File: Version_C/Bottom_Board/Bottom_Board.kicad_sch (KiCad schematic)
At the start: 9 parts, among them J1 Conn_02x03_Top_Bottom, J2 Conn_02x03_Top_Bottom, J3 Screw_Terminal_01x06, J5 DIN-5, SW2 SW_DIP_x04

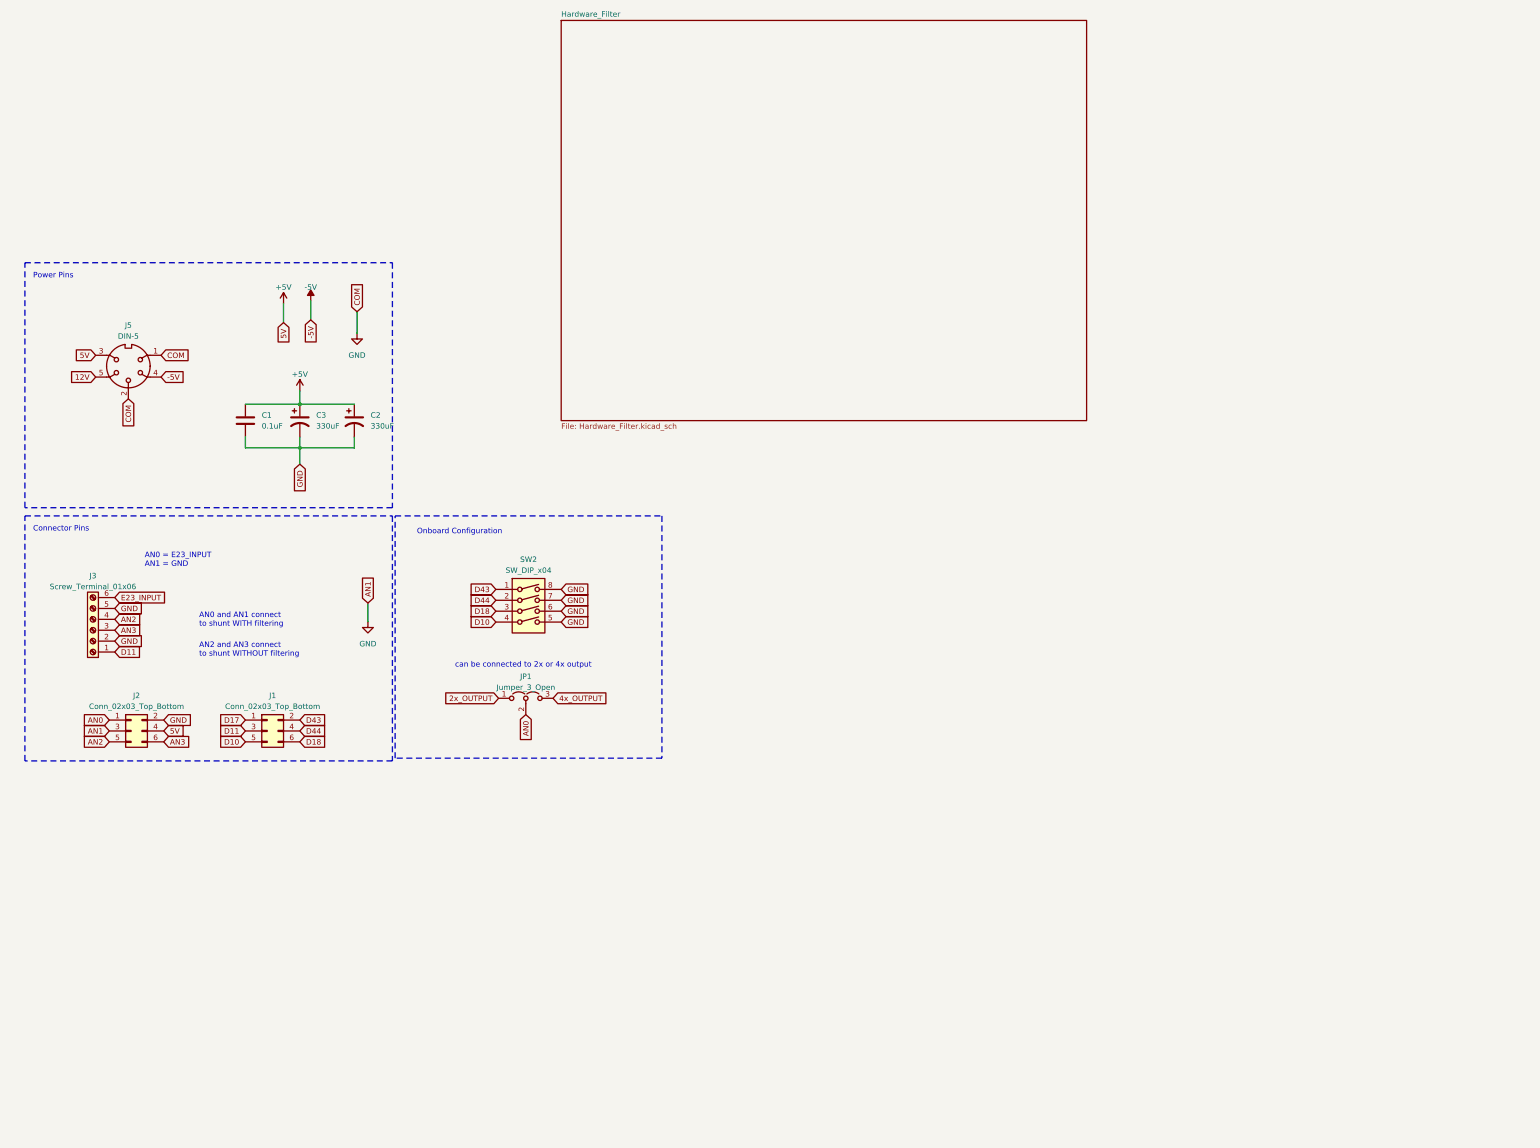
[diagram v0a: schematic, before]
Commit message: fixed directory overwrite
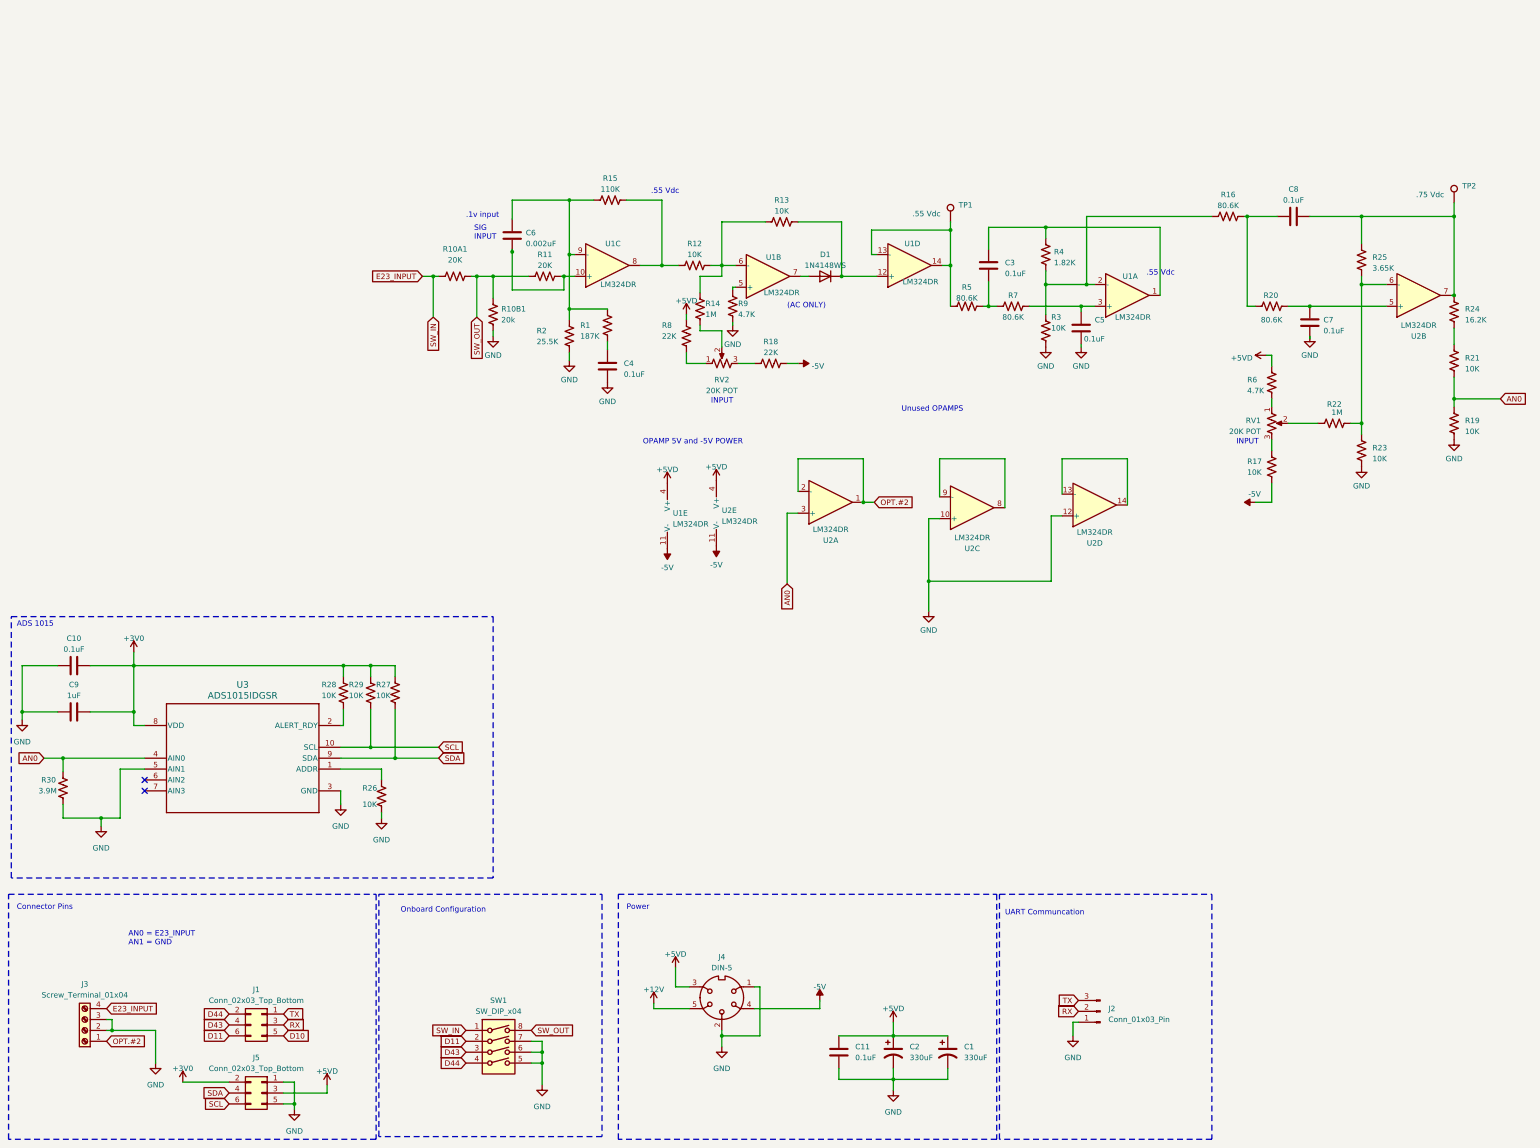
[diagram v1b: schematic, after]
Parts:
- removed J3: Screw_Terminal_01x06, Connector_Phoenix_MSTB:PhoenixContact_MSTBA_2,5_6-G-5,08_1x06_P5.08mm_Horizontal, symbol Connector:Screw_Terminal_01x06
- removed JP1: Jumper_3_Open, Connector_PinHeader_2.54mm:PinHeader_1x03_P2.54mm_Vertical, symbol Jumper:Jumper_3_Open
- added C10, C3, C4, C5, C7, C8: 0.1uF, Capacitor_SMD:C_0603_1608Metric, symbol Device:C
- added C6: 0.002uF, Capacitor_SMD:C_0603_1608Metric, symbol Device:C
- added C9: 1uF, Capacitor_SMD:C_0603_1608Metric, symbol Device:C
- added D1: 1N4148WS, bot_lib:Diode_1N4148WS, symbol Diode:1N914
- added J2: Conn_01x03_Pin, Connector_PinHeader_2.54mm:PinHeader_1x03_P2.54mm_Vertical, symbol Connector:Conn_01x03_Pin
- added J3: Screw_Terminal_01x04, bot_lib:Terminal_Strip_4_Pin, symbol Connector:Screw_Terminal_01x04
- added R1: 187K, Resistor_SMD:R_0603_1608Metric, symbol Device:R_US
- added R10A1, R11: 20K, Resistor_SMD:R_0603_1608Metric, symbol Device:R_US
- added R10B1: 20k, Resistor_SMD:R_0603_1608Metric, symbol Device:R_US
- added R12, R13, R17, R19, R21, R23, R26, R27, R28, R29, R3: 10K, Resistor_SMD:R_0603_1608Metric, symbol Device:R_US
- added R14, R22: 1M, Resistor_SMD:R_0603_1608Metric, symbol Device:R_US
- added R15: 110K, Resistor_SMD:R_0603_1608Metric, symbol Device:R_US
- added R16, R20, R5, R7: 80.6K, Resistor_SMD:R_0603_1608Metric, symbol Device:R_US
- added R18, R8: 22K, Resistor_SMD:R_0603_1608Metric, symbol Device:R_US
- added R2: 25.5K, Resistor_SMD:R_0603_1608Metric, symbol Device:R_US
- added R24: 16.2K, Resistor_SMD:R_0603_1608Metric, symbol Device:R_US
- added R25: 3.65K, Resistor_SMD:R_0603_1608Metric, symbol Device:R_US
- added R30: 3.9M, Resistor_SMD:R_0603_1608Metric, symbol Device:R_US
- added R4: 1.82K, Resistor_SMD:R_0603_1608Metric, symbol Device:R_US
- added R6, R9: 4.7K, Resistor_SMD:R_0603_1608Metric, symbol Device:R_US
- added RV1, RV2: 20K POT, bot_lib:Potentiometer_Bourns_3386P_Vertical, symbol Device:R_Potentiometer_US
- added TP1: .55 Vdc, TestPoint:TestPoint_Loop_D2.54mm_Drill1.5mm_Beaded, symbol Connector:TestPoint
- added TP2: .75 Vdc, TestPoint:TestPoint_Loop_D2.54mm_Drill1.5mm_Beaded, symbol Connector:TestPoint
- added U1, U2: LM324DR, Package_SO:SOIC-14_3.9x8.7mm_P1.27mm, symbol Amplifier_Operational:LM324
- added U3: ADS1015IDGSR, bot_lib:DGS0010A_N, symbol ads1015:ADS1015IDGSR
- J1: renamed from J2; footprint Connector_PinSocket_2.54mm:PinSocket_2x03_P2.54mm_Vertical -> bot_lib:PinSocket_2x03_P2.54mm_Vertical
- J5: renamed from J1; footprint Connector_PinSocket_2.54mm:PinSocket_2x03_P2.54mm_Vertical -> bot_lib:PinSocket_2x03_P2.54mm_Vertical
- renumbered C2 to C1, C1 to C11, C3 to C2, J5 to J4, SW2 to SW1
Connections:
- net AN2 is gone; now on net D10: J1.5 (Pin_5)
- net AN3 is gone; now on net D11: J1.6 (Pin_6)
- net D17 is gone; now on net GND: J5.1 (Pin_1)
- net -5V: now also R17.1, R18.2, U1.11 (V-), U2.11 (V-)
- net AN0: now also R19.2, R21.1, R30.1, U2.3 (+), U3.4 (AIN0); no longer J1.1 (Pin_1)
- net D10: no longer J5.5 (Pin_5), SW1.4
- net D11: now also SW1.2; no longer J5.3 (Pin_3)
- net D43: now also J1.4 (Pin_4), SW1.3; no longer J5.2 (Pin_2), SW1.1
- net D44: now also J1.2 (Pin_2), SW1.4; no longer J5.4 (Pin_4), SW1.2
- net E23_INPUT: now also SW1.1, J3.4 (Pin_4), R10A1.1
- net GND: now also J5.5 (Pin_5), C10.1, C4.2, C5.2, C7.1, C9.1, J2.1 (Pin_1), J3.2 (Pin_2), J3.3 (Pin_3), R10B1.2, R19.1, R2.2, R23.1, R26.2, R3.2, R30.2, R9.2, U2.10 (+), U2.12 (+), U3.3 (GND), U3.5 (AIN1); no longer J1.2 (Pin_2), J1.3 (Pin_3), SW1.8
- net +5V renamed +5VD
- net +5VD: now also J5.3 (Pin_3), R6.2, R8.1, U1.4 (V+), U2.4 (V+); no longer J1.4 (Pin_4)
- net 12V renamed +12V
- net D18 renamed SCL
- net SCL: now also R29.2, U3.10 (SCL); no longer SW1.3
- new net: R9.1, U1.5 (+)
- new net: R12.2, R13.1, R14.1, U1.6 (-)
- new net: D1.2 (A), U1.7
- new net: C6.2, R11.2, U1.10 (+)
- new net: R12.1, R15.2, U1.8
- new net: C6.1, R1.1, R15.1, R2.1, U1.9 (-)
- new net: R21.2, R24.1
- new net: C7.2, R20.2, U2.5 (+)
- new net: C3.2, R5.2, R7.1
- new net: C5.1, R7.2, U1.3 (+)
- new net: R6.1, RV1.1
- new net: R22.2, RV1.2
- new net: R17.2, RV1.3
- new net: R26.1, U3.1 (ADDR)
- new net: R28.2, U3.2 (ALERT_RDY)
- new net: R22.1, R23.2, R25.1, U2.6 (-)
- new net: R8.2, RV2.1
- new net: C8.2, R16.1, R20.1
- new net: R18.1, RV2.3
- new net: R14.2, RV2.2
- new net: C8.1, R24.2, R25.2, TP2.1, U2.7
- new net: D1.1 (K), R13.2, U1.12 (+)
- new net: R5.1, TP1.1, U1.13 (-), U1.14
- new net: C3.1, R4.2, U1.1
- new net: R16.2, R3.1, R4.1, U1.2 (-)
- new net: U2.13 (-), U2.14
- new net: C4.1, R1.2
- new net: U2.8, U2.9 (-)
- new net +3V0: C10.2, C9.2, J5.2 (Pin_2), R27.1, R28.1, R29.1, U3.8 (VDD)
- new net OPT.#2: J3.1 (Pin_1), U2.1, U2.2 (-)
- new net RX: J1.3 (Pin_3), J2.2 (Pin_2)
- new net SDA: J5.4 (Pin_4), R27.2, U3.9 (SDA)
- new net SW_OUT: R10A1.2, R10B1.1, R11.1, SW1.8
- new net TX: J1.1 (Pin_1), J2.3 (Pin_3)
- no-connect marks 0 -> 2
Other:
- removed sheet Hardware_Filter
- note added: "(AC ONLY)"
- note added: ".1v input"
- note added: ".55 Vdc"
- note added: "ADS 1015"
- note added: "INPUT"
- note added: "OPAMP 5V and -5V POWER"
- note added: "Power"
- note added: "SIG INPUT"
- note added: "UART Communcation"
- note added: "Unused OPAMPS"
- note removed: "AN0 and AN1 connect to shunt WITH filtering"
- note removed: "AN2 and AN3 connect to shunt WITHOUT filtering"
- note removed: "Power Pins"
- note removed: "can be connected to 2x or 4x output"
- company: (none) -> Secured Solutions Group
- title: (none) -> Current Monitoring System (Bottom Board)
- moved on the sheet: C1, C11, C2, J1, J4, J5, SW1
